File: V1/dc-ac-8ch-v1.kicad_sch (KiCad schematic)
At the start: 102 parts, among them J1 DB142V-5.08-4P, J2 DB142V-5.08-4P, J3 DB142V-5.08-2P, J4 DB142V-5.08-4P, J5 DB142V-5.08-4P, J6 DB142V-5.08-2P, U1 MOC3063S, U2 MOC3063S, U3 MOC3063S, U4 MOC3063S, U5 MOC3063S, U6 MOC3063S, U7 MOC3063S, U8 MOC3063S

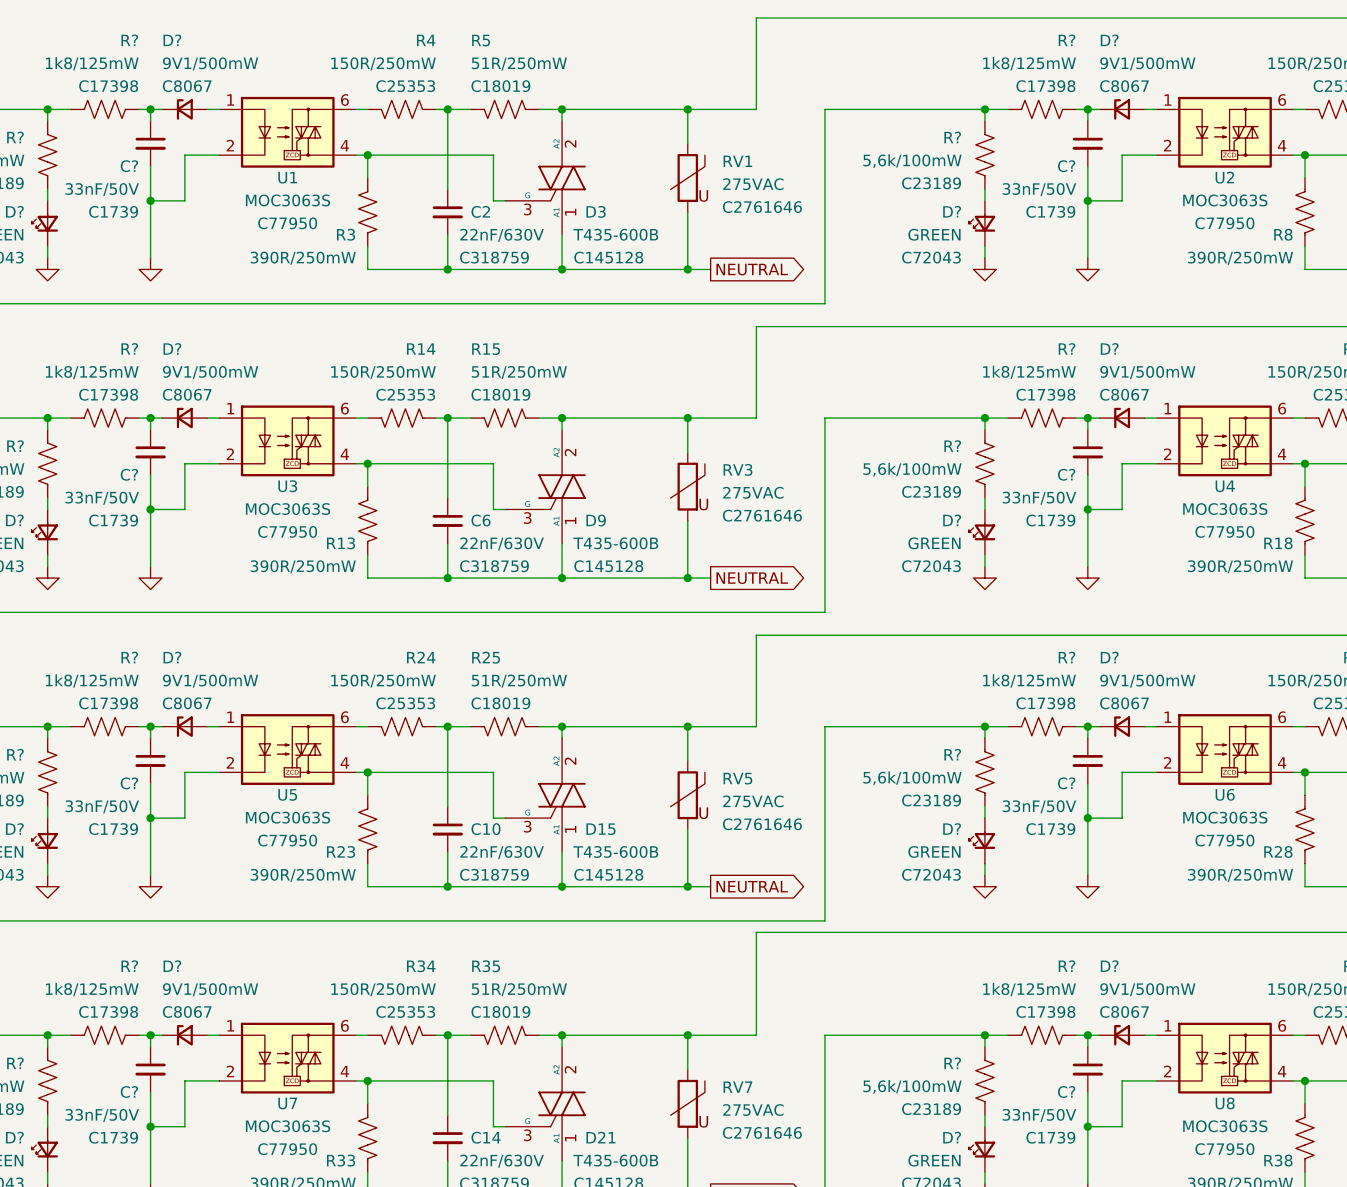
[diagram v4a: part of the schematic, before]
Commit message: Zener diode replaced
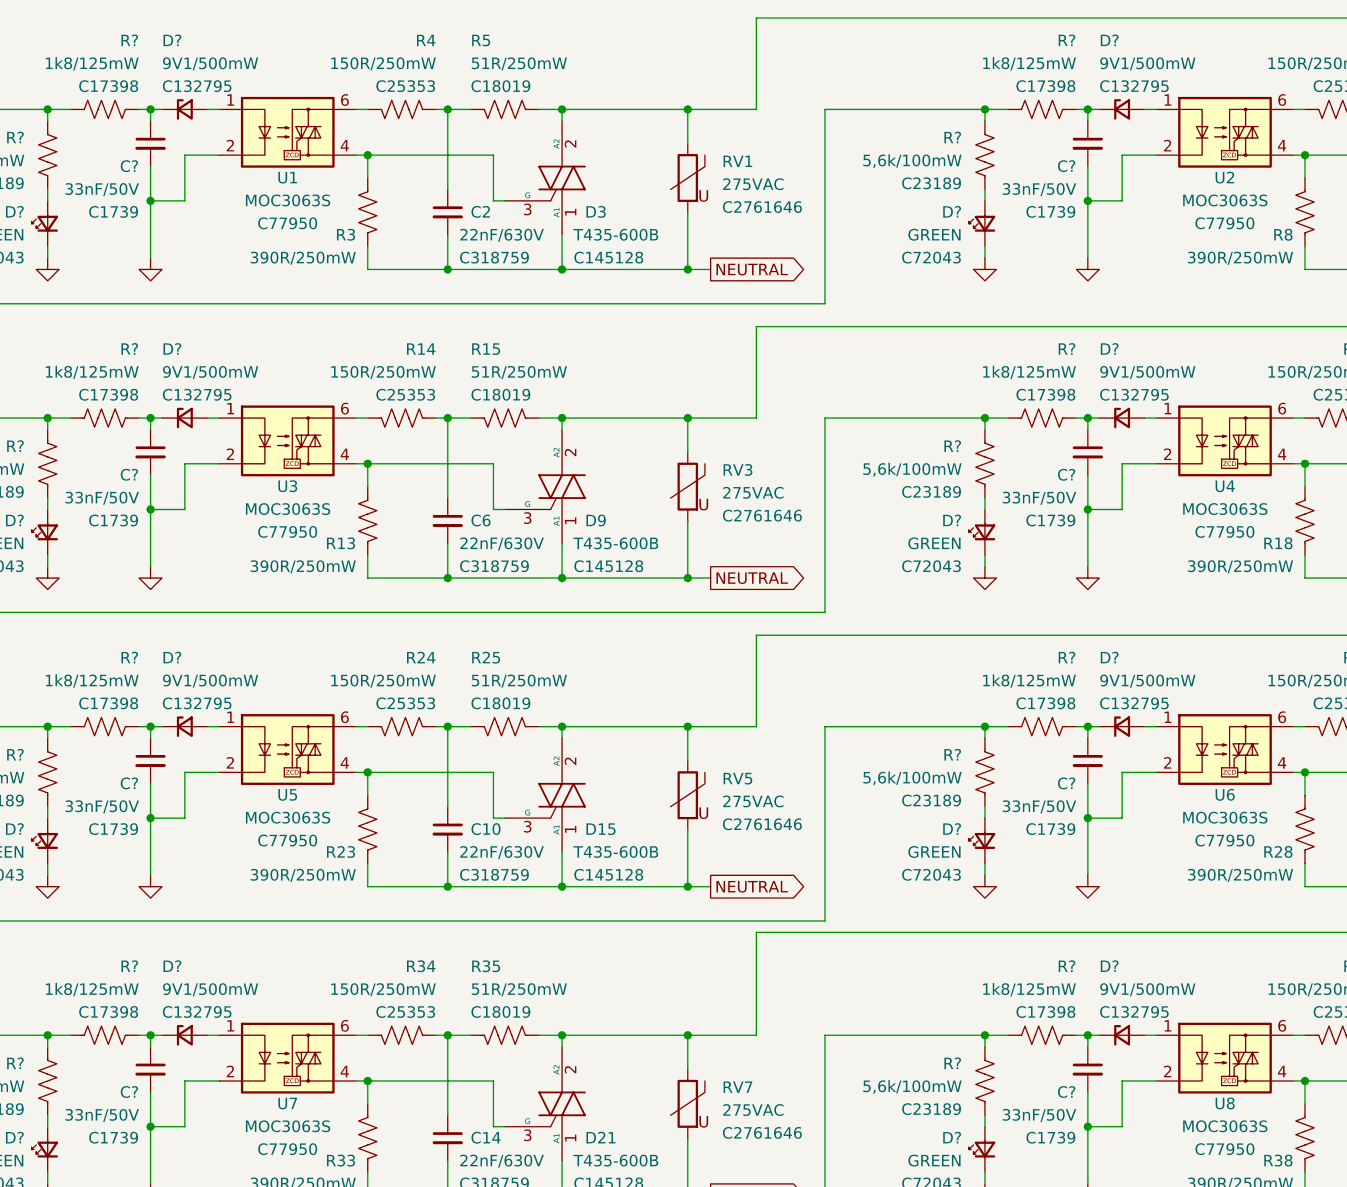
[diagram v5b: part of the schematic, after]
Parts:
- D? (x8): footprint Tales:D_MiniMELF -> Tales:D_SOD-123; LCSC Part # C8067 -> C132795; Mfr ST(Semtech) -> onsemi; Mfr Part # ZMM9V1-M -> MMSZ9V1T1G; Package Mini-MELF -> SOD-123; Vendor Part # C8067 -> C132795
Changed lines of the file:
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@@
       (effects (font (size 1.27 1.27)) (justify left))
     )
-    (property "Footprint" "Tales:D_MiniMELF" (at 74.93 29.21 90)
+    (property "Footprint" "Tales:D_SOD-123" (at 74.93 29.21 90)
       (effects (font (size 1.27 1.27)) hide)
     )
@@
       (effects (font (size 1.27 1.27)) hide)
     )
-    (property "Mfr" "ST(Semtech)" (at 74.93 29.21 0)
+    (property "Mfr" "onsemi" (at 74.93 29.21 0)
       (effects (font (size 1.27 1.27)) hide)
     )
@@
       (effects (font (size 1.27 1.27)) hide)
     )
-    (property "LCSC Part #" "C8067" (at 72.39 26.67 0)
+    (property "LCSC Part #" "C132795" (at 72.39 26.67 0)
       (effects (font (size 1.27 1.27)) (justify left))
     )
-    (property "Vendor Part #" "C8067" (at 74.93 29.21 0)
+    (property "Vendor Part #" "C132795" (at 74.93 29.21 0)
       (effects (font (size 1.27 1.27)) hide)
     )
-    (property "Package" "Mini-MELF" (at 74.93 29.21 0)
+    (property "Package" "SOD-123" (at 74.93 29.21 0)
       (effects (font (size 1.27 1.27)) hide)
     )
-    (property "Mfr Part #" "ZMM9V1-M" (at 74.93 29.21 0)
+    (property "Mfr Part #" "MMSZ9V1T1G" (at 74.93 29.21 0)
       (effects (font (size 1.27 1.27)) hide)
     )
@@
       (effects (font (size 1.27 1.27)) (justify left))
     )
-    (property "Footprint" "Tales:D_MiniMELF" (at 74.93 132.08 90)
+    (property "Footprint" "Tales:D_SOD-123" (at 74.93 132.08 90)
       (effects (font (size 1.27 1.27)) hide)
     )
@@
       (effects (font (size 1.27 1.27)) hide)
     )
-    (property "Mfr" "ST(Semtech)" (at 74.93 132.08 0)
+    (property "Mfr" "onsemi" (at 74.93 132.08 0)
       (effects (font (size 1.27 1.27)) hide)
     )
@@
       (effects (font (size 1.27 1.27)) hide)
     )
-    (property "LCSC Part #" "C8067" (at 72.39 129.54 0)
+    (property "LCSC Part #" "C132795" (at 72.39 129.54 0)
       (effects (font (size 1.27 1.27)) (justify left))
     )
-    (property "Vendor Part #" "C8067" (at 74.93 132.08 0)
+    (property "Vendor Part #" "C132795" (at 74.93 132.08 0)
       (effects (font (size 1.27 1.27)) hide)
     )
-    (property "Package" "Mini-MELF" (at 74.93 132.08 0)
+    (property "Package" "SOD-123" (at 74.93 132.08 0)
       (effects (font (size 1.27 1.27)) hide)
     )
-    (property "Mfr Part #" "ZMM9V1-M" (at 74.93 132.08 0)
+    (property "Mfr Part #" "MMSZ9V1T1G" (at 74.93 132.08 0)
       (effects (font (size 1.27 1.27)) hide)
     )
@@
       (effects (font (size 1.27 1.27)) (justify left))
     )
-    (property "Footprint" "Tales:D_MiniMELF" (at 74.93 97.79 90)
+    (property "Footprint" "Tales:D_SOD-123" (at 74.93 97.79 90)
       (effects (font (size 1.27 1.27)) hide)
     )
@@
       (effects (font (size 1.27 1.27)) hide)
     )
-    (property "Mfr" "ST(Semtech)" (at 74.93 97.79 0)
+    (property "Mfr" "onsemi" (at 74.93 97.79 0)
       (effects (font (size 1.27 1.27)) hide)
     )
@@
       (effects (font (size 1.27 1.27)) hide)
     )
-    (property "LCSC Part #" "C8067" (at 72.39 95.25 0)
+    (property "LCSC Part #" "C132795" (at 72.39 95.25 0)
       (effects (font (size 1.27 1.27)) (justify left))
     )
-    (property "Vendor Part #" "C8067" (at 74.93 97.79 0)
+    (property "Vendor Part #" "C132795" (at 74.93 97.79 0)
       (effects (font (size 1.27 1.27)) hide)
     )
-    (property "Package" "Mini-MELF" (at 74.93 97.79 0)
+    (property "Package" "SOD-123" (at 74.93 97.79 0)
       (effects (font (size 1.27 1.27)) hide)
     )
-    (property "Mfr Part #" "ZMM9V1-M" (at 74.93 97.79 0)
+    (property "Mfr Part #" "MMSZ9V1T1G" (at 74.93 97.79 0)
       (effects (font (size 1.27 1.27)) hide)
     )
@@
       (effects (font (size 1.27 1.27)) (justify left))
     )
-    (property "Footprint" "Tales:D_MiniMELF" (at 74.93 63.5 90)
+    (property "Footprint" "Tales:D_SOD-123" (at 74.93 63.5 90)
       (effects (font (size 1.27 1.27)) hide)
     )
@@
       (effects (font (size 1.27 1.27)) hide)
     )
-    (property "Mfr" "ST(Semtech)" (at 74.93 63.5 0)
+    (property "Mfr" "onsemi" (at 74.93 63.5 0)
       (effects (font (size 1.27 1.27)) hide)
     )
@@
       (effects (font (size 1.27 1.27)) hide)
     )
-    (property "LCSC Part #" "C8067" (at 72.39 60.96 0)
+    (property "LCSC Part #" "C132795" (at 72.39 60.96 0)
       (effects (font (size 1.27 1.27)) (justify left))
     )
-    (property "Vendor Part #" "C8067" (at 74.93 63.5 0)
+    (property "Vendor Part #" "C132795" (at 74.93 63.5 0)
       (effects (font (size 1.27 1.27)) hide)
     )
-    (property "Package" "Mini-MELF" (at 74.93 63.5 0)
+    (property "Package" "SOD-123" (at 74.93 63.5 0)
       (effects (font (size 1.27 1.27)) hide)
     )
-    (property "Mfr Part #" "ZMM9V1-M" (at 74.93 63.5 0)
+    (property "Mfr Part #" "MMSZ9V1T1G" (at 74.93 63.5 0)
       (effects (font (size 1.27 1.27)) hide)
     )
@@
       (effects (font (size 1.27 1.27)) (justify left))
     )
-    (property "Footprint" "Tales:D_MiniMELF" (at 179.07 97.79 90)
+    (property "Footprint" "Tales:D_SOD-123" (at 179.07 97.79 90)
       (effects (font (size 1.27 1.27)) hide)
     )
@@
       (effects (font (size 1.27 1.27)) hide)
     )
-    (property "Mfr" "ST(Semtech)" (at 179.07 97.79 0)
+    (property "Mfr" "onsemi" (at 179.07 97.79 0)
       (effects (font (size 1.27 1.27)) hide)
     )
@@
       (effects (font (size 1.27 1.27)) hide)
     )
-    (property "LCSC Part #" "C8067" (at 176.53 95.25 0)
+    (property "LCSC Part #" "C132795" (at 176.53 95.25 0)
       (effects (font (size 1.27 1.27)) (justify left))
     )
-    (property "Vendor Part #" "C8067" (at 179.07 97.79 0)
+    (property "Vendor Part #" "C132795" (at 179.07 97.79 0)
       (effects (font (size 1.27 1.27)) hide)
     )
-    (property "Package" "Mini-MELF" (at 179.07 97.79 0)
+    (property "Package" "SOD-123" (at 179.07 97.79 0)
       (effects (font (size 1.27 1.27)) hide)
     )
-    (property "Mfr Part #" "ZMM9V1-M" (at 179.07 97.79 0)
+    (property "Mfr Part #" "MMSZ9V1T1G" (at 179.07 97.79 0)
       (effects (font (size 1.27 1.27)) hide)
     )
@@
       (effects (font (size 1.27 1.27)) (justify left))
     )
-    (property "Footprint" "Tales:D_MiniMELF" (at 179.07 132.08 90)
+    (property "Footprint" "Tales:D_SOD-123" (at 179.07 132.08 90)
       (effects (font (size 1.27 1.27)) hide)
     )
@@
       (effects (font (size 1.27 1.27)) hide)
     )
-    (property "Mfr" "ST(Semtech)" (at 179.07 132.08 0)
+    (property "Mfr" "onsemi" (at 179.07 132.08 0)
       (effects (font (size 1.27 1.27)) hide)
     )
@@
       (effects (font (size 1.27 1.27)) hide)
     )
-    (property "LCSC Part #" "C8067" (at 176.53 129.54 0)
+    (property "LCSC Part #" "C132795" (at 176.53 129.54 0)
       (effects (font (size 1.27 1.27)) (justify left))
     )
-    (property "Vendor Part #" "C8067" (at 179.07 132.08 0)
+    (property "Vendor Part #" "C132795" (at 179.07 132.08 0)
       (effects (font (size 1.27 1.27)) hide)
     )
-    (property "Package" "Mini-MELF" (at 179.07 132.08 0)
+    (property "Package" "SOD-123" (at 179.07 132.08 0)
       (effects (font (size 1.27 1.27)) hide)
     )
-    (property "Mfr Part #" "ZMM9V1-M" (at 179.07 132.08 0)
+    (property "Mfr Part #" "MMSZ9V1T1G" (at 179.07 132.08 0)
       (effects (font (size 1.27 1.27)) hide)
     )
@@
       (effects (font (size 1.27 1.27)) (justify left))
     )
-    (property "Footprint" "Tales:D_MiniMELF" (at 179.07 29.21 90)
+    (property "Footprint" "Tales:D_SOD-123" (at 179.07 29.21 90)
       (effects (font (size 1.27 1.27)) hide)
     )
@@
       (effects (font (size 1.27 1.27)) hide)
     )
-    (property "Mfr" "ST(Semtech)" (at 179.07 29.21 0)
+    (property "Mfr" "onsemi" (at 179.07 29.21 0)
       (effects (font (size 1.27 1.27)) hide)
     )
@@
       (effects (font (size 1.27 1.27)) hide)
     )
-    (property "LCSC Part #" "C8067" (at 176.53 26.67 0)
+    (property "LCSC Part #" "C132795" (at 176.53 26.67 0)
       (effects (font (size 1.27 1.27)) (justify left))
     )
-    (property "Vendor Part #" "C8067" (at 179.07 29.21 0)
+    (property "Vendor Part #" "C132795" (at 179.07 29.21 0)
       (effects (font (size 1.27 1.27)) hide)
     )
-    (property "Package" "Mini-MELF" (at 179.07 29.21 0)
+    (property "Package" "SOD-123" (at 179.07 29.21 0)
       (effects (font (size 1.27 1.27)) hide)
     )
-    (property "Mfr Part #" "ZMM9V1-M" (at 179.07 29.21 0)
+    (property "Mfr Part #" "MMSZ9V1T1G" (at 179.07 29.21 0)
       (effects (font (size 1.27 1.27)) hide)
     )
@@
       (effects (font (size 1.27 1.27)) (justify left))
     )
-    (property "Footprint" "Tales:D_MiniMELF" (at 179.07 63.5 90)
+    (property "Footprint" "Tales:D_SOD-123" (at 179.07 63.5 90)
       (effects (font (size 1.27 1.27)) hide)
     )
@@
       (effects (font (size 1.27 1.27)) hide)
     )
-    (property "Mfr" "ST(Semtech)" (at 179.07 63.5 0)
+    (property "Mfr" "onsemi" (at 179.07 63.5 0)
       (effects (font (size 1.27 1.27)) hide)
     )
@@
       (effects (font (size 1.27 1.27)) hide)
     )
-    (property "LCSC Part #" "C8067" (at 176.53 60.96 0)
+    (property "LCSC Part #" "C132795" (at 176.53 60.96 0)
       (effects (font (size 1.27 1.27)) (justify left))
     )
-    (property "Vendor Part #" "C8067" (at 179.07 63.5 0)
+    (property "Vendor Part #" "C132795" (at 179.07 63.5 0)
       (effects (font (size 1.27 1.27)) hide)
     )
-    (property "Package" "Mini-MELF" (at 179.07 63.5 0)
+    (property "Package" "SOD-123" (at 179.07 63.5 0)
       (effects (font (size 1.27 1.27)) hide)
     )
-    (property "Mfr Part #" "ZMM9V1-M" (at 179.07 63.5 0)
+    (property "Mfr Part #" "MMSZ9V1T1G" (at 179.07 63.5 0)
       (effects (font (size 1.27 1.27)) hide)
     )

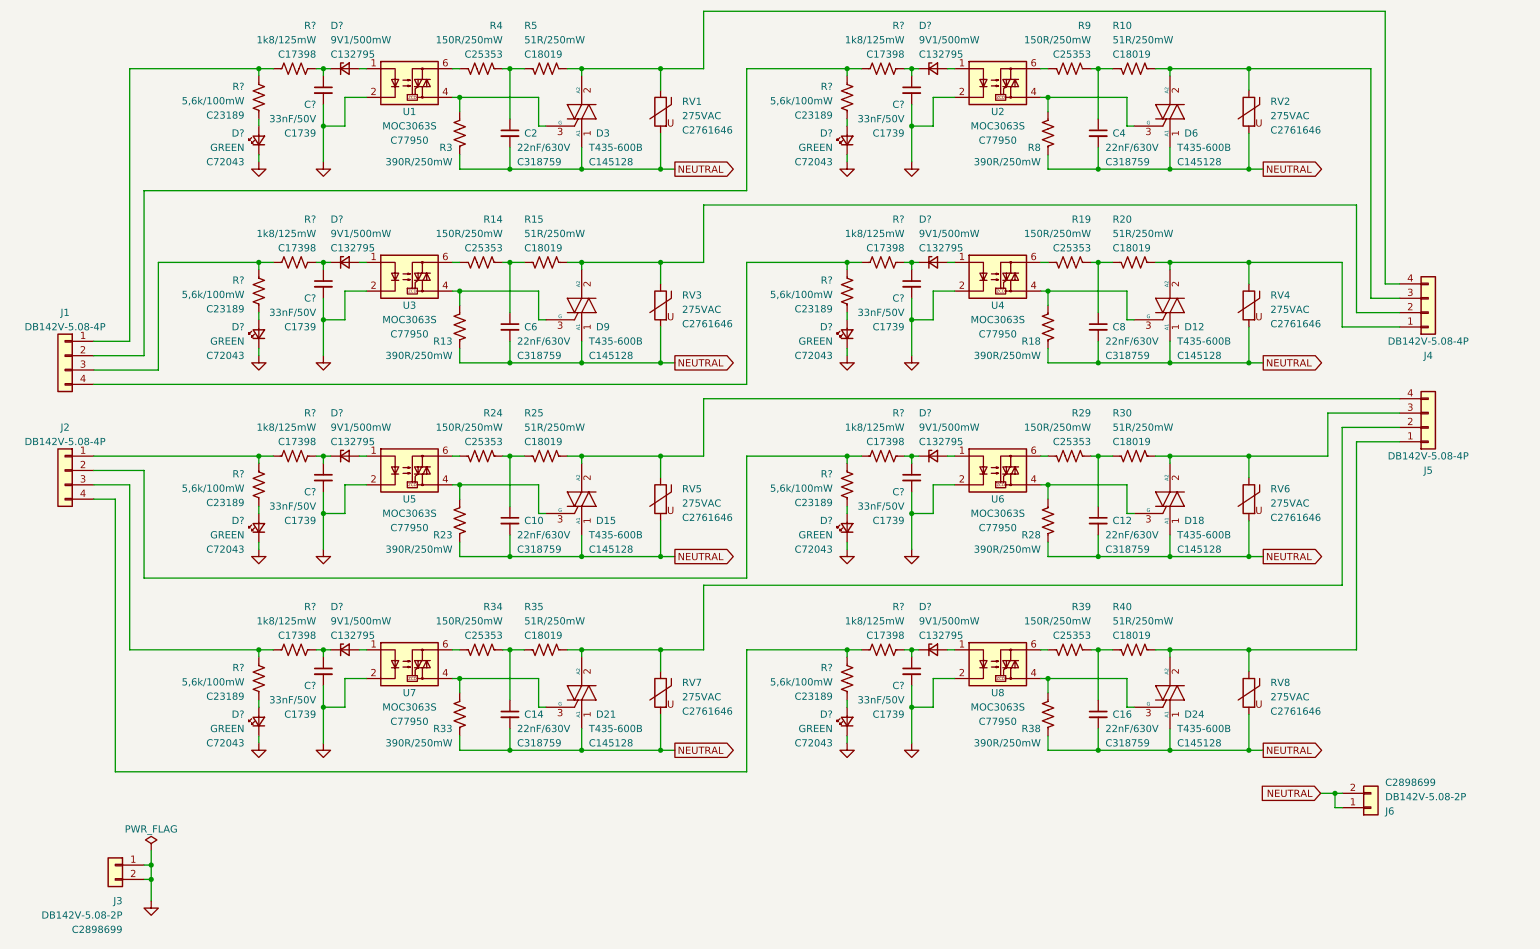
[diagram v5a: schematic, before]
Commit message: Replace resistor for basic part
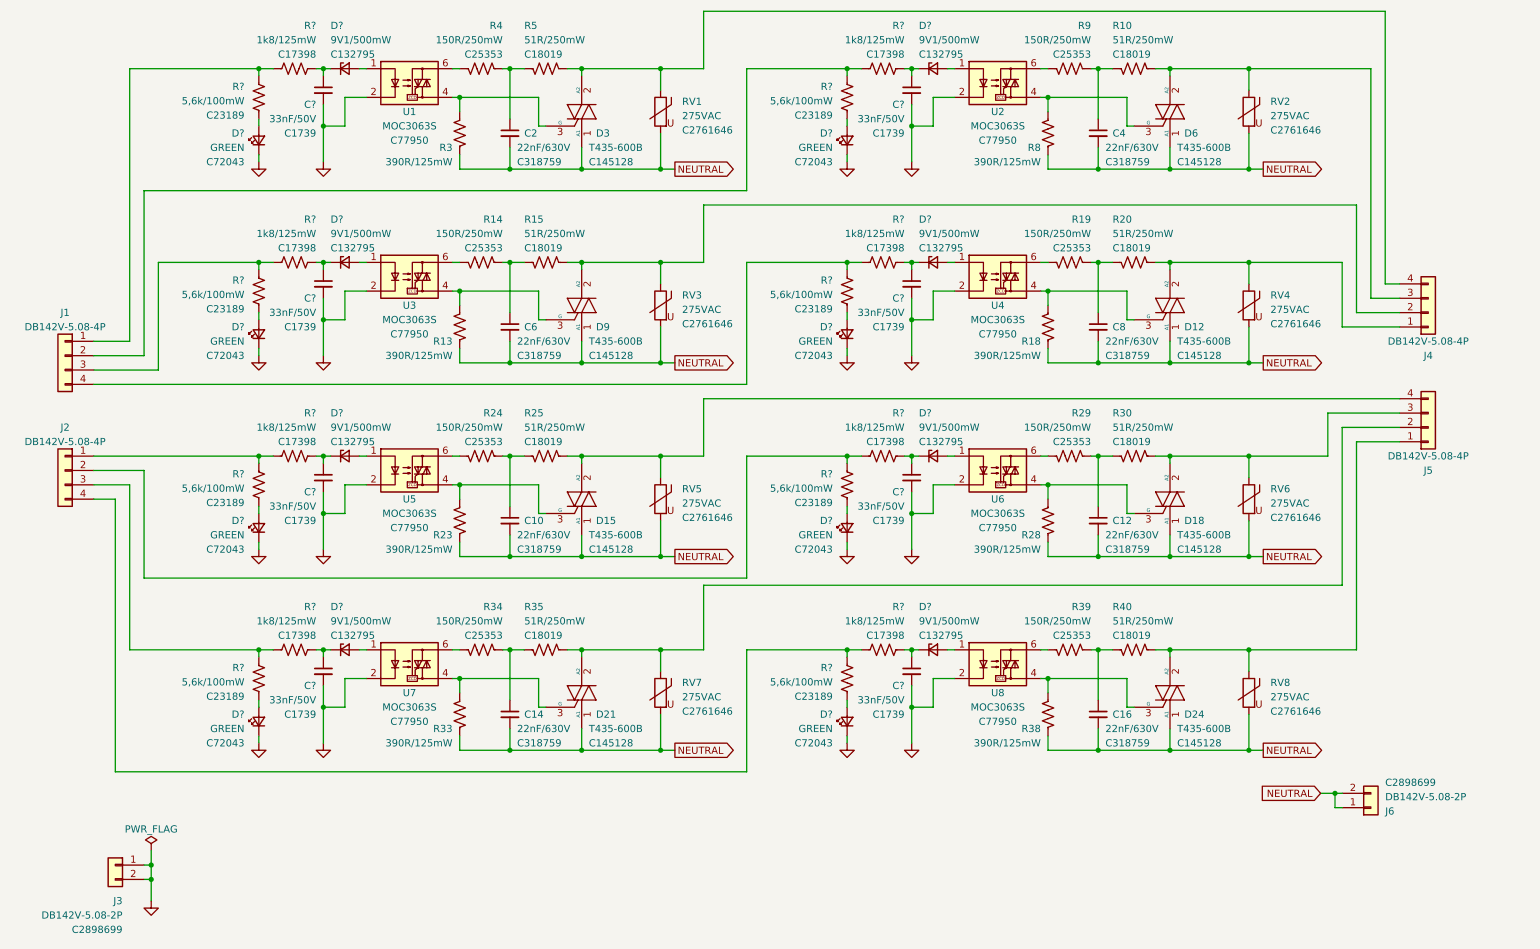
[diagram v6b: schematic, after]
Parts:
- R13, R18, R23, R28, R3, R33, R38, R8: value 390R/250mW -> 390R/125mW; footprint Tales:R_1206_3216Metric -> Tales:R_0805_2012Metric; LCSC Part # C25378 -> C17655; Mfr Part # 1206W4J0391T5E -> 0805W8F3900T5E; Package 1206/3216 -> 0805/2012; Vendor Part # C25378 -> C17655
